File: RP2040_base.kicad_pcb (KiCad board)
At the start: 2 copper layers, 27 parts, among them J2 Conn_01x02, U1 W25Q16JV, U4 RP2040, U6 LM1117-3.3, Y2 ECS-120-8-33-JGN-TR3

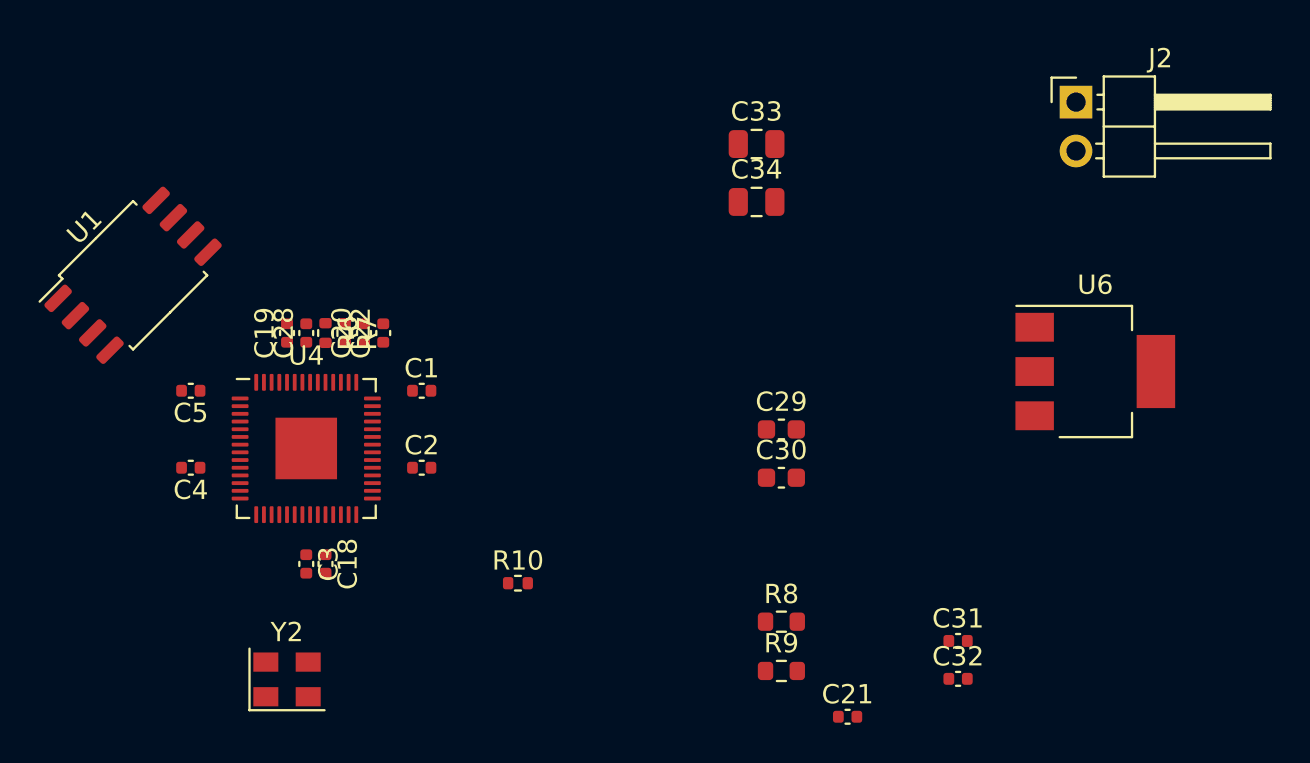
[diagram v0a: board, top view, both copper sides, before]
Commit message: Create sample pcb layout, manage schematic files better, and fill in missing 3d model.
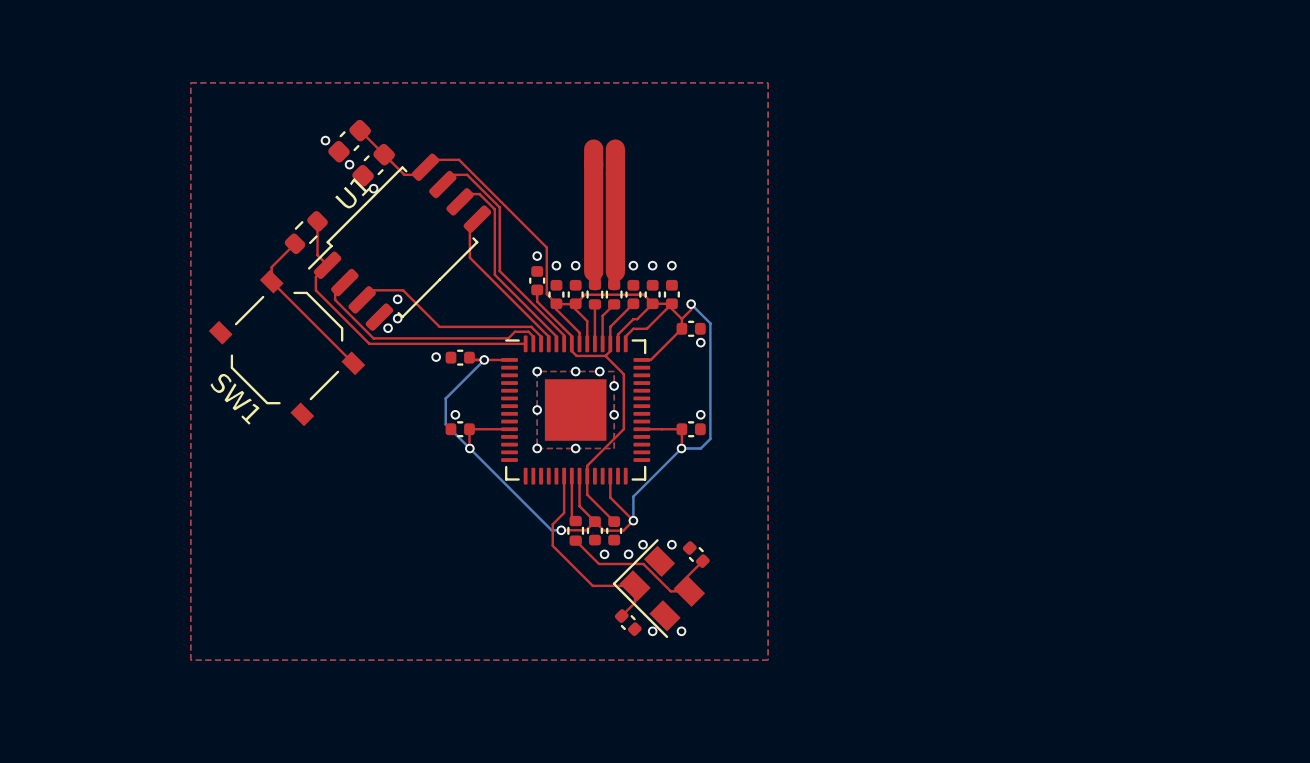
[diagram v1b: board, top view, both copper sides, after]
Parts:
- removed C20, C22: 1u, Capacitor_SMD:C_0402_1005Metric
- removed C21: 100n, Capacitor_SMD:C_0402_1005Metric
- removed C33, C34: 10u, Capacitor_SMD:C_0805_2012Metric
- removed J2: Conn_01x02, Connector_PinHeader_2.54mm:PinHeader_1x02_P2.54mm_Horizontal
- removed R9: DNF, Resistor_SMD:R_0603_1608Metric
- removed U4: RP2040, Package_DFN_QFN:QFN-56-1EP_7x7mm_P0.4mm_EP3.2x3.2mm
- removed U6: LM1117-3.3, Package_TO_SOT_SMD:SOT-223-3_TabPin2
- added C6: 1u, Capacitor_SMD:C_0402_1005Metric, F.Cu at (38.0, 31.0)
- added C7: 1u, Capacitor_SMD:C_0402_1005Metric, F.Cu at (39.0, 31.0)
- added C8: 100n, Capacitor_SMD:C_0402_1005Metric, F.Cu at (40.0, 31.0)
- added C9: 100n, Capacitor_SMD:C_0402_1005Metric, F.Cu at (35.0, 31.0)
- added SW1: SW_Push, RP2040_base:TS-1187A, F.Cu at (20.0, 33.8)
- added U2: RP2040, Package_DFN_QFN:QFN-56-1EP_7x7mm_P0.4mm_EP3.2x3.2mm, F.Cu at (35.0, 37.0)
- U1: footprint Package_SO:SOIC-8_5.23x5.23mm_P1.27mm -> Package_SO:SOIC-8_5.275x5.275mm_P1.27mm
- moved R8 31.9 mm to (21.0, 27.8), turned to -135 degrees
- moved C29 27.0 mm to (23.2, 23.0), turned to -135 degrees
- moved C30 26.7 mm to (24.5, 24.3), turned to -135 degrees
- moved Y2 20.1 mm to (39.5, 46.3), turned to -45 degrees
- moved C31 17.2 mm to (37.7, 48.0), turned to -45 degrees
- moved C18 15.1 mm to (37.0, 43.3)
- moved C3 15.1 mm to (36.0, 43.3)
- moved C32 15.1 mm to (41.3, 44.5), turned to 135 degrees
- moved C1 14.4 mm to (41.0, 32.8)
- moved C2 14.1 mm to (41.0, 38.0)
- moved C4 14.1 mm to (29.0, 38.0)
- moved R6 14.1 mm to (36.0, 31.0)
- moved R7 14.1 mm to (37.0, 31.0)
- moved C5 14.1 mm to (29.0, 34.3)
- moved U1 14.1 mm to (26.0, 28.3)
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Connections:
- net +3V3_L renamed /VIN
- net GND_L renamed /GND
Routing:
- net /VIN: track 0.00 -> 84.2 mm, vias 0 -> 6
- net /1V1: track 0.00 -> 19.5 mm
- net /QSPI_SS: track 0.00 -> 16.1 mm
- net /QSPI_SD1: track 0.00 -> 12.9 mm
- net /QSPI_SD3: track 0.00 -> 12.3 mm
- net /QSPI_SD2: track 0.00 -> 10.9 mm
- net /XIN: track 0.00 -> 10.9 mm
- net /QSPI_SCLK: track 0.00 -> 10.6 mm
- net Net-(C32-Pad1): track 0.00 -> 9.02 mm
- net /~{USB_BOOT}: track 0.00 -> 8.47 mm
- net /QSPI_SD0: track 0.00 -> 8.34 mm
- net /USB_D-: track 0.00 -> 7.08 mm
- net /USB_D+: track 0.00 -> 7.08 mm
- net /XOUT: track 0.00 -> 2.42 mm
- net Net-(U2-USB_DM): track 0.00 -> 2.30 mm
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- added copper zone on B.Cu, net /GND
- added copper zone on F.Cu, net /GND
